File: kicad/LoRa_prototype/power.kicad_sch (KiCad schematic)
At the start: 44 parts, among them J2 USB_C_Receptacle_PowerOnly_6P, J3 BAT, U2 BQ24074RGTT

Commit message: Done schematic for GPS and gas sensors (Milestone)
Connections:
- net BAT+: now also R10.1, U3.3 (VDD)
- net OUT: no longer R10.1, U3.3 (VDD)
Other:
- moved on the sheet: C27, C28, C29, D1, J2, R4, R5, R6, R7, R8, R9, TP2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

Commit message: Schematic cleanup (0 ERC violations)
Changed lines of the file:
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@@
 	)
 	(hierarchical_label "SCL_FG"
-		(shape bidirectional)
+		(shape input)
 		(at 109.22 63.5 0)
 		(effects

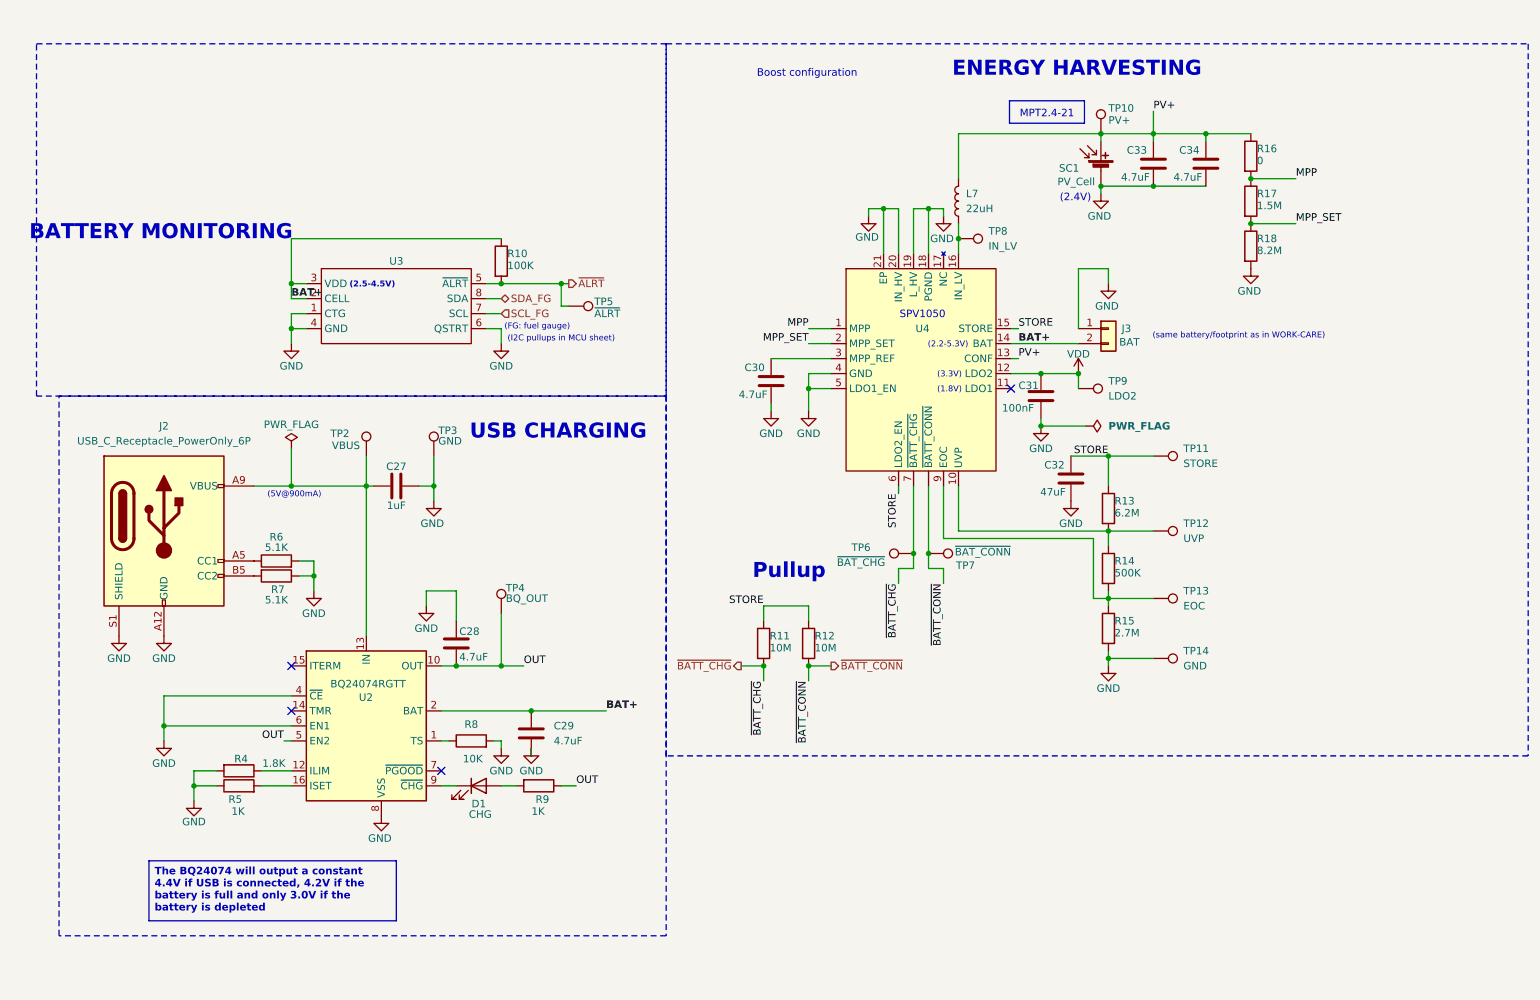
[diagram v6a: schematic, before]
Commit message: Added pin headers in schematics
To activate/deactivate subsystems as well as measure currents
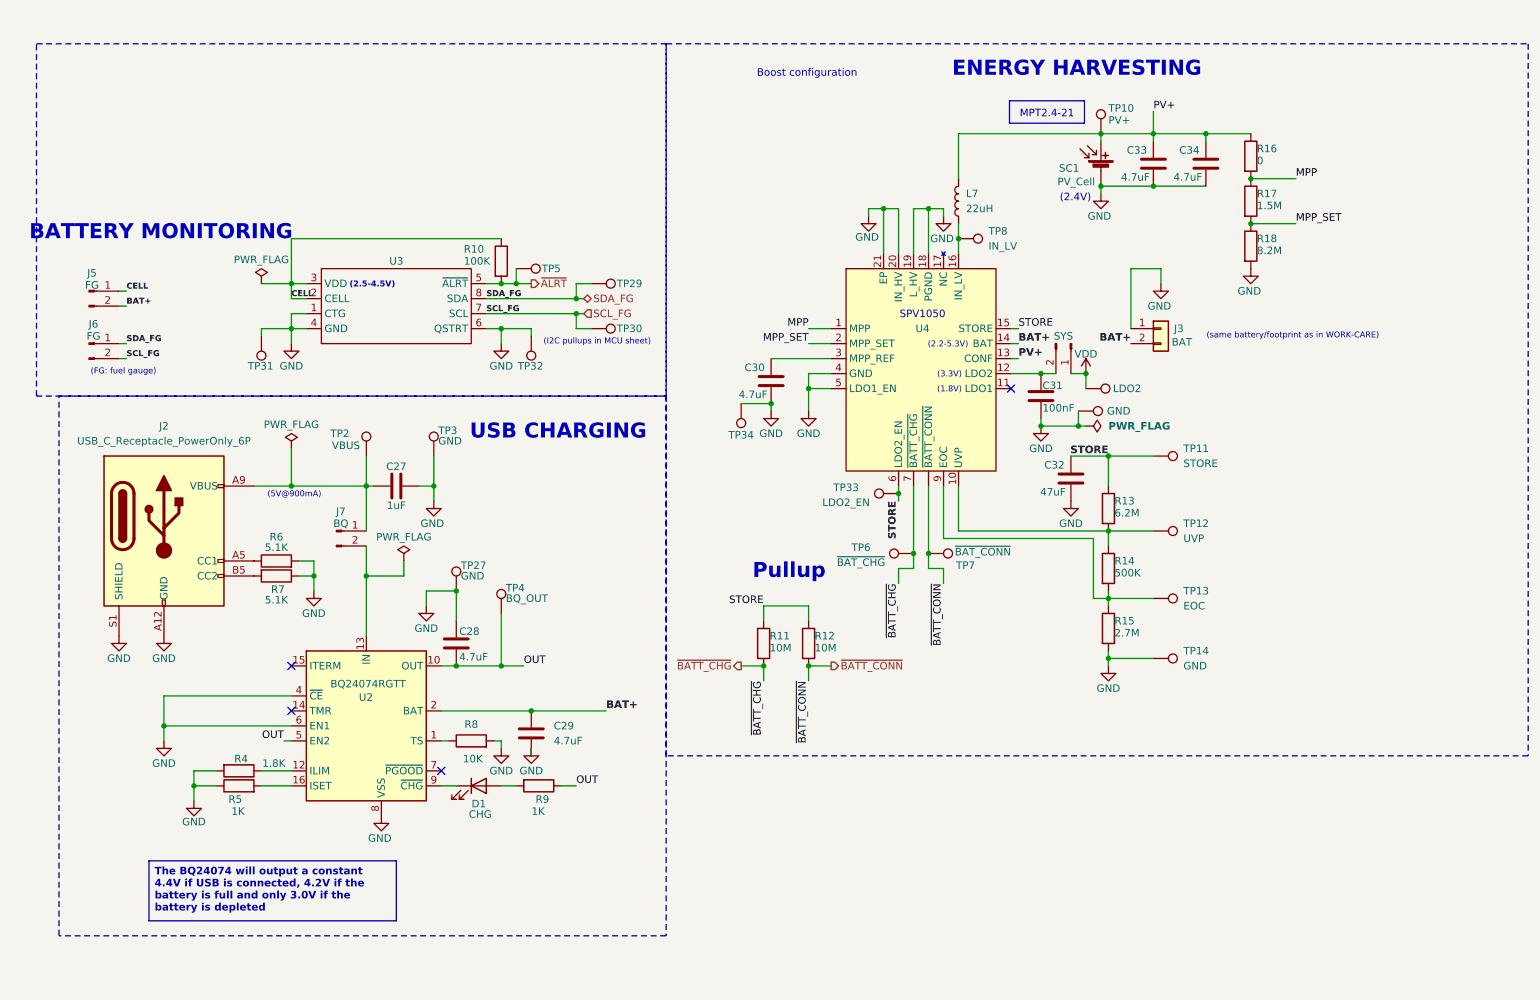
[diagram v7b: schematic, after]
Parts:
- added J15: SYS, Connector_PinHeader_2.54mm:PinHeader_1x02_P2.54mm_Vertical, symbol Connector:Conn_01x02_Pin
- added J5, J6: FG, Connector_PinHeader_2.54mm:PinHeader_1x02_P2.54mm_Vertical, symbol Connector:Conn_01x02_Pin
- added J7: BQ, Connector_PinHeader_2.54mm:PinHeader_1x02_P2.54mm_Vertical, symbol Connector:Conn_01x02_Pin
- added TP27, TP28, TP31, TP32, TP34: GND, TestPoint:TestPoint_Pad_2.0x2.0mm, symbol Connector:TestPoint
- added TP29: SDA_FG, TestPoint:TestPoint_Pad_2.0x2.0mm, symbol Connector:TestPoint
- added TP30: SCL_FG, TestPoint:TestPoint_Pad_2.0x2.0mm, symbol Connector:TestPoint
- added TP33: LDO2_EN, TestPoint:TestPoint_Pad_2.0x2.0mm, symbol Connector:TestPoint
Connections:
- net BAT+: now also J5.2 (Pin_2); no longer R10.1, U3.2 (CELL), U3.3 (VDD)
- net GND: now also TP27.1, TP28.1, TP31.1, TP32.1, TP34.1
- net SCL_FG: now also J6.2 (Pin_2), TP30.1
- net SDA_FG: now also J6.1 (Pin_1), TP29.1
- net STORE: now also TP33.1
- net VDD: now also J15.1 (Pin_1); no longer C31.1, U4.12 (LDO2)
- net at C27.1, J2.A9 (VBUS), J2.B9 (VBUS)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: now also J7.1 (Pin_1); no longer U2.13 (IN)
- new net: J7.2 (Pin_2), U2.13 (IN)
- new net: C31.1, J15.2 (Pin_2), U4.12 (LDO2)
- new net CELL: J5.1 (Pin_1), R10.1, U3.2 (CELL), U3.3 (VDD)
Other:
- moved on the sheet: J3, TP5

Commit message: Created separate folders for footprints and 3d models
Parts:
- C27, C28, C29: footprint Capacitor_SMD:C_0603_1608Metric -> Capacitor_SMD:C_0805_2012Metric
- C30, C31, C32, C33, C34: footprint (none) -> Capacitor_SMD:C_0805_2012Metric
- D1: footprint LED_SMD:LED_0603_1608Metric -> LED_SMD:LED_0805_2012Metric
- R10, R11, R12, R13, R14, R15, R16, R17, R18, R6, R7: footprint (none) -> Resistor_SMD:R_0805_2012Metric
- R4, R5, R8, R9: footprint Resistor_SMD:R_0603_1608Metric -> Resistor_SMD:R_0805_2012Metric
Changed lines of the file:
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@@
 			)
 		)
-		(property "Footprint" ""
+		(property "Footprint" "Resistor_SMD:R_0805_2012Metric"
 			(at 71.12 106.172 90)
 			(effects
@@
 			)
 		)
-		(property "Footprint" ""
+		(property "Footprint" "Resistor_SMD:R_0805_2012Metric"
 			(at 210.312 106.68 90)
 			(effects
@@
 			)
 		)
-		(property "Footprint" ""
+		(property "Footprint" "Resistor_SMD:R_0805_2012Metric"
 			(at 159.512 119.38 90)
 			(effects
@@
 			)
 		)
-		(property "Footprint" ""
+		(property "Footprint" "Resistor_SMD:R_0805_2012Metric"
 			(at 234.442 52.07 90)
 			(effects
@@
 			)
 		)
-		(property "Footprint" "LED_SMD:LED_0603_1608Metric"
+		(property "Footprint" "LED_SMD:LED_0805_2012Metric"
 			(at 105.41 143.51 0)
 			(effects
@@
 			)
 		)
-		(property "Footprint" ""
+		(property "Footprint" "Resistor_SMD:R_0805_2012Metric"
 			(at 151.892 119.38 90)
 			(effects
@@
 			)
 		)
-		(property "Footprint" ""
+		(property "Footprint" "Capacitor_SMD:C_0805_2012Metric"
 			(at 218.7448 34.29 0)
 			(effects
@@
 			)
 		)
-		(property "Footprint" ""
+		(property "Footprint" "Resistor_SMD:R_0805_2012Metric"
 			(at 234.442 36.83 90)
 			(effects
@@
 			)
 		)
-		(property "Footprint" ""
+		(property "Footprint" "Capacitor_SMD:C_0805_2012Metric"
 			(at 227.6348 34.29 0)
 			(effects
@@
 			)
 		)
-		(property "Footprint" ""
+		(property "Footprint" "Capacitor_SMD:C_0805_2012Metric"
 			(at 204.7748 87.63 0)
 			(effects
@@
 			)
 		)
-		(property "Footprint" "Capacitor_SMD:C_0603_1608Metric"
+		(property "Footprint" "Capacitor_SMD:C_0805_2012Metric"
 			(at 100.6348 115.57 0)
 			(effects
@@
 			)
 		)
-		(property "Footprint" ""
+		(property "Footprint" "Resistor_SMD:R_0805_2012Metric"
 			(at 107.442 54.61 90)
 			(effects
@@
 			)
 		)
-		(property "Footprint" ""
+		(property "Footprint" "Resistor_SMD:R_0805_2012Metric"
 			(at 71.12 107.188 90)
 			(effects
@@
 			)
 		)
-		(property "Footprint" ""
+		(property "Footprint" "Resistor_SMD:R_0805_2012Metric"
 			(at 210.312 96.52 90)
 			(effects
@@
 			)
 		)
-		(property "Footprint" "Resistor_SMD:R_0603_1608Metric"
+		(property "Footprint" "Resistor_SMD:R_0805_2012Metric"
 			(at 64.77 145.288 90)
 			(effects
@@
 			)
 		)
-		(property "Footprint" "Resistor_SMD:R_0603_1608Metric"
+		(property "Footprint" "Resistor_SMD:R_0805_2012Metric"
 			(at 115.57 141.732 90)
 			(effects
@@
 			)
 		)
-		(property "Footprint" "Capacitor_SMD:C_0603_1608Metric"
+		(property "Footprint" "Capacitor_SMD:C_0805_2012Metric"
 			(at 113.3348 130.81 0)
 			(effects
@@
 			)
 		)
-		(property "Footprint" "Resistor_SMD:R_0603_1608Metric"
+		(property "Footprint" "Resistor_SMD:R_0805_2012Metric"
 			(at 64.77 139.192 90)
 			(effects
@@
 			)
 		)
-		(property "Footprint" ""
+		(property "Footprint" "Capacitor_SMD:C_0805_2012Metric"
 			(at 153.9748 71.12 0)
 			(effects
@@
 			)
 		)
-		(property "Footprint" ""
+		(property "Footprint" "Resistor_SMD:R_0805_2012Metric"
 			(at 234.442 44.45 90)
 			(effects
@@
 			)
 		)
-		(property "Footprint" ""
+		(property "Footprint" "Resistor_SMD:R_0805_2012Metric"
 			(at 210.312 116.84 90)
 			(effects
@@
 			)
 		)
-		(property "Footprint" ""
+		(property "Footprint" "Capacitor_SMD:C_0805_2012Metric"
 			(at 201.6252 81.28 0)
 			(effects
@@
 			)
 		)
-		(property "Footprint" "Resistor_SMD:R_0603_1608Metric"
+		(property "Footprint" "Resistor_SMD:R_0805_2012Metric"
 			(at 104.14 137.668 90)
 			(effects
@@
 			)
 		)
-		(property "Footprint" "Capacitor_SMD:C_0603_1608Metric"
+		(property "Footprint" "Capacitor_SMD:C_0805_2012Metric"
 			(at 95.25 91.7448 0)
 			(effects
